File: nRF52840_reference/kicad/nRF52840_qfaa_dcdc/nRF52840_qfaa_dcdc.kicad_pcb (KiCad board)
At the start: 2 copper layers, 45 x 45 mm, 33 parts, among them J1 CONN_COAXIAL, U1 nRF52840, X1 XTAL_32MHZ, X2 XTAL_32KHZ

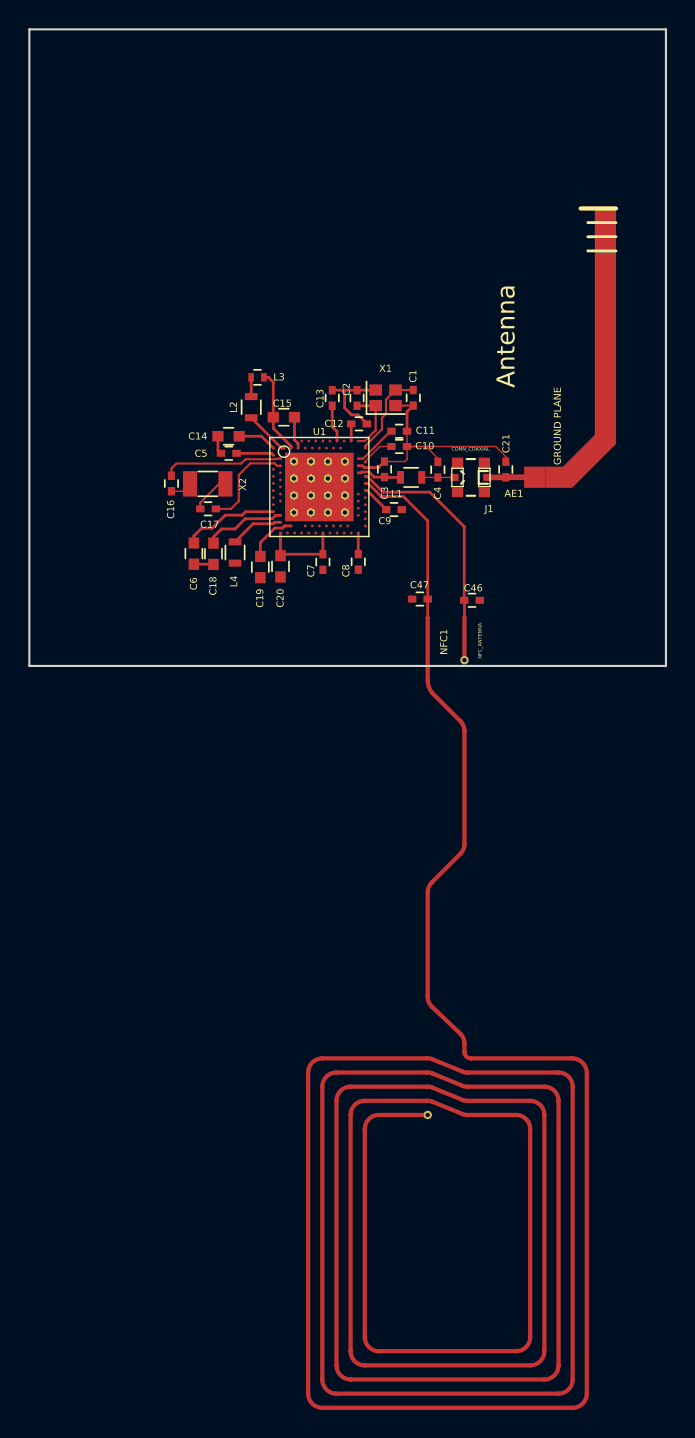
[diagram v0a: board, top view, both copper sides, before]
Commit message: Update KiCAD Project nRF52840_qfaa_dcdc
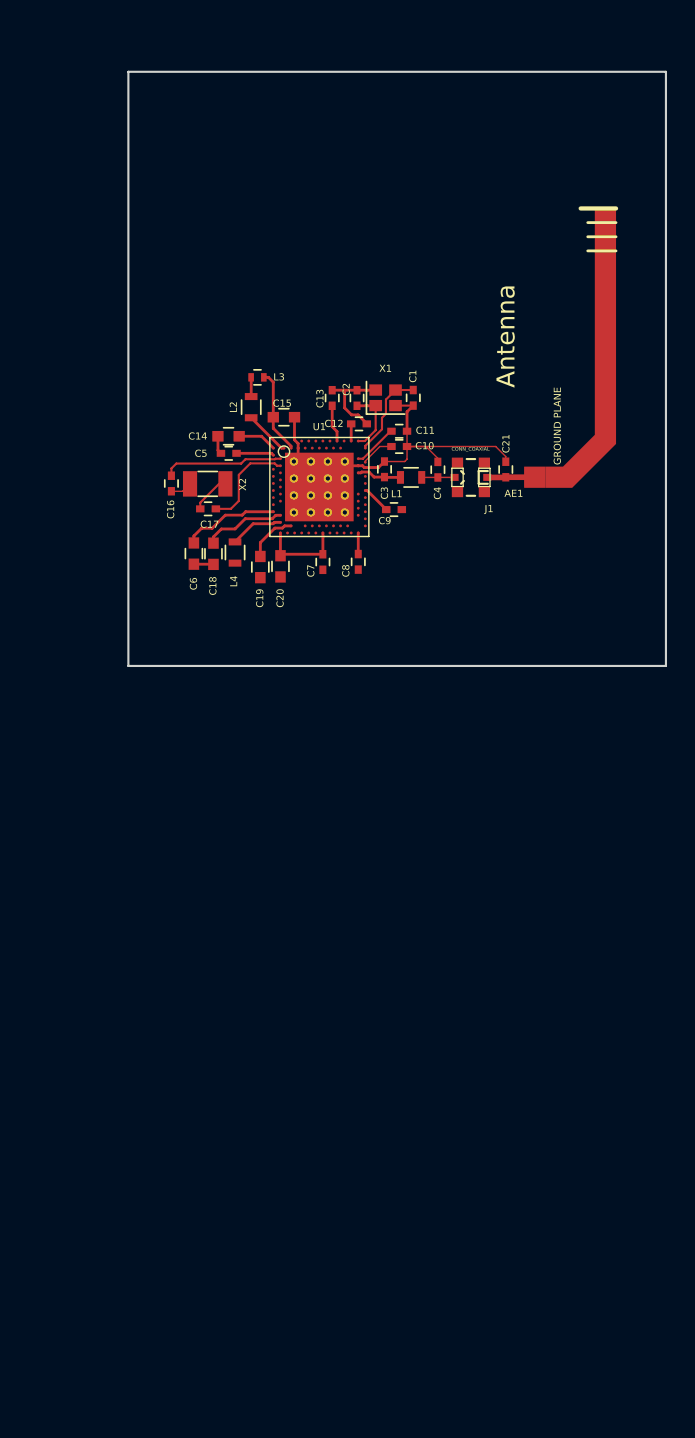
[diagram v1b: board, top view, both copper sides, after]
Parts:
- removed C46, C47: 300pF, Nordic_misc:C_0402
- removed NFC1: NFC_ANTENNA, Nordic_misc:Nordic_misc-NFC_ANT
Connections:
- U1 pad 74: Net-(U1-Pad74) -> GND
- U1 pad J24: /NFC2 -> (no net)
- U1 pad L24: /NFC1 -> (no net)
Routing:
- net /NFC2: track 14.9 -> 0.00 mm
- net /NFC1: track 12.4 -> 0.00 mm
- net GND: track 30.7 -> 37.5 mm
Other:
- board size 45 x 45 mm -> 38 x 42 mm
